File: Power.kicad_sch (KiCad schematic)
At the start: 16 parts, among them Q1 PMH950UPEH, U5 AP63205WU-7, U7 MCP1700T-3302E/TT

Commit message: 2nd rev schematic done
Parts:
- removed C10, C9: 1uF, Capacitor_SMD:C_0402_1005Metric, symbol Device:C_Small
- removed C4: 100nF, Capacitor_SMD:C_0402_1005Metric, symbol Device:C_Small
- removed C6, C7: 22uF, Capacitor_SMD:C_0805_2012Metric, symbol Device:C_Small
- removed U5: AP63205WU-7, SproutSenseFootprints:SOIC_05WU-7_DIO, symbol SproutSense:AP63205WU-7
- removed U7: MCP1700T-3302E/TT, SproutSenseFootprints:SOT-23_MC_MCH, symbol SproutSense:MCP1700T-3302E_TT
- added C11, C15, C16, C5: 22uF, Capacitor_SMD:C_0805_2012Metric, symbol Device:C_Small
- added C17: 10n, Capacitor_SMD:C_0201_0603Metric, symbol Device:C_Small
- added L3: 2.2u, SproutSenseFootprints:IND_VLS3012CX-2R2M-1, symbol Device:L_Small
- added R13: 9.31k, Resistor_SMD:R_0402_1005Metric, symbol Device:R_Small_US
- added R15: 7.5k, Resistor_SMD:R_0402_1005Metric, symbol Device:R_Small_US
- added R16, R22: 100k, Resistor_SMD:R_0402_1005Metric, symbol Device:R_US
- added R17: 154k, Resistor_SMD:R_0402_1005Metric, symbol Device:R_US
- added R21: 249k, Resistor_SMD:R_0402_1005Metric, symbol Device:R_US
- added R23, R24: 34k, Resistor_SMD:R_0402_1005Metric, symbol Device:R_US
- added U6: TPS629203DRL, SproutSenseFootprints:SOT5X3-8_DRL_TEX, symbol SproutSense:TPS629203DRL
- added U9: TPS629206DRLR, SOT5X3-8_DRL_TEX, symbol SproutSense:TPS629206DRLR
- C3: value 22uF -> 10n; footprint Capacitor_SMD:C_0805_2012Metric -> Capacitor_SMD:C_0201_0603Metric; Distributor Prt # 490-GRM21BZ71A226ME15LCT-ND -> 490-3194-1-ND; Manuf Prt # GRM21BZ71A226ME15L -> GRM033R71A103KA01D
- L1: value 4.7uH -> 2.2u; footprint SproutSenseFootprints:IND_TAIYO_NRS6028_TAY -> SproutSenseFootprints:IND_VLS3012CX-2R2M-1; Distributor Prt # 587-2943-1-ND -> 445-180922-1-ND; Manuf Prt # NRS6028T4R7MMGK -> VLS3012CX-2R2M-1
- R7: value 4.7k -> 7.5k; Distributor Prt # 311-4.7KJRCT-ND -> 311-7.50KLRCT-ND; Manuf Prt # RC0402JR-074K7L -> RC0402FR-077K5L
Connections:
- net +3V3: now also C3.1, L1.2, C11.1, R16.2, R17.1, U6.3 (VOS)
- net +5V: now also C16.1, C17.1, L3.2, R21.1, R22.2, U9.3 (VOS); no longer L1.2
- net +BATT: now also C15.1, C5.1, U6.6 (VIN), U6.7 (EN), U9.6 (VIN); no longer C3.1
- net GND: now also C11.2, C15.2, C16.2, C17.2, C5.2, R13.1, R15.1, R23.2, R24.2, U6.5 (GND), U9.5 (GND)
- net at L1.1: now also U6.4 (SW)
- new net: R17.2, R24.1, U6.1 (FB/VSET)
- new net: R21.2, R23.1, U9.1 (FB/VSET)
- new net: R22.1, U9.2 (PG)
- new net: L3.1, U9.4 (SW)
- new net: R13.2, U9.8 (MODE/S-CONF)
- new net: R16.1, U6.2 (PG)
- new net: R15.2, U6.8 (MODE/S-CONF)
- new net PWR_ENA_5p0: U9.7 (EN)
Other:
- note added: "Li-Ion 18650 Batt 7.2V Nom Voltage"
- note added: "Max Voltage = 8.4V 8.4 * (4.7 / 12.2) = 3.24"
- note removed: "X7R"
- moved on the sheet: BT2, BT3, D11, Q1, R8, R9

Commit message: mostly routed
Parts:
- removed BT2, BT3: Battery_Cell, SproutSenseFootprints:Keystone_18650_Holder, symbol Device:Battery_Cell
- added J1: S2B-PH-K-S, SproutSenseFootprints:CONN_S2B-PH-K-S_JST, symbol Connector:Conn_01x02_Socket
- added TP14, TP15: TestPoint, TestPoint:TestPoint_Pad_D1.0mm, symbol Connector:TestPoint
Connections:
- net +3V3: now also TP14.1
- net +5V: now also TP15.1
- net BAT_POS: now also J1.2 (Pin_2)
- net GND: now also J1.1 (Pin_1)
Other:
- note added: "2S 7.4V LiPo Battery"
- note removed: "Li-Ion 18650 Batt 7.2V Nom Voltage"
- moved on the sheet: D11, Q1, R7, R8, R9

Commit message: edited silksceen
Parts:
- added TP7: TestPoint, TestPoint:TestPoint_Pad_D1.0mm, symbol Connector:TestPoint
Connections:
- net GND: now also TP7.1
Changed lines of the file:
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@@
+	)
+	(junction
+		(at 199.39 120.65)
+		(diameter 0)
+		(color 0 0 0 0)
 	)
 	(junction
@@
 		(pts
 			(xy 67.31 99.06) (xy 67.31 104.14)
+		)
+		(stroke
+			(width 0)
+			(type default)
+		)
+	)
+	(wire
+		(pts
+			(xy 199.39 107.95) (xy 199.39 120.65)
 		)
 		(stroke
@@
 					(unit 1)
 				)
+			)
+		)
+	)
+	(symbol
+		(lib_id "Connector:TestPoint")
+		(at 199.39 107.95 0)
+		(unit 1)
+		(exclude_from_sim no)
+		(in_bom yes)
+		(on_board yes)
+		(dnp no)
+		(property "Reference" "TP7"
+			(at 197.866 102.87 0)
+			(effects
+				(font
+					(size 1.27 1.27)
+				)
+				(justify left)
+			)
+		)
+		(property "Value" "TestPoint"
+			(at 201.93 105.9179 0)
+			(effects
+				(font
+					(size 1.27 1.27)
+				)
+				(justify left)
+				(hide yes)
+			)
+		)
+		(property "Footprint" "TestPoint:TestPoint_Pad_D1.0mm"
+			(at 204.47 107.95 0)
+			(effects
+				(font
+					(size 1.27 1.27)
+				)
+				(hide yes)
+			)
+		)
+		(property "Datasheet" "~"
+			(at 204.47 107.95 0)
+			(effects
+				(font
+					(size 1.27 1.27)
+				)
+				(hide yes)
+			)
+		)
+		(property "Description" "test point"
+			(at 199.39 107.95 0)
+			(effects
+				(font
+					(size 1.27 1.27)
+				)
+				(hide yes)
+			)
+		)
+		(property "MAXIMUM_PACKAGE_HEIGHT" ""
+			(at 199.39 107.95 0)
+			(effects
+				(font
+					(size 1.27 1.27)
+				)
+				(hide yes)
+			)
+		)
+		(pin "1"
+		)
+		(instances
+			(project "SproutSync_SensorNode"
+				(path "/6b347550-6a02-4d2d-97d7-e1cbb1403859/8aac59c9-744f-46ff-a9bf-5095a50423d5"
+					(reference "TP7")
+					(unit 1)
+				)

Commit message: finished rev1
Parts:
- removed TP14, TP15: TestPoint, TestPoint:TestPoint_Pad_D1.0mm, symbol Connector:TestPoint
- added R25: 100m, Resistor_SMD:R_0603_1608Metric, symbol Device:R_Small_US
- added TP11, TP8: TestPoint, TestPoint:TestPoint_Pad_D1.0mm, symbol Connector:TestPoint
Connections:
- net +BATT: now also R25.2, TP11.1; no longer D11.1
- new net: D11.1, R25.1, TP8.1
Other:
- note added: "rsense for power testing"
- moved on the sheet: C11, C16, C17, C3

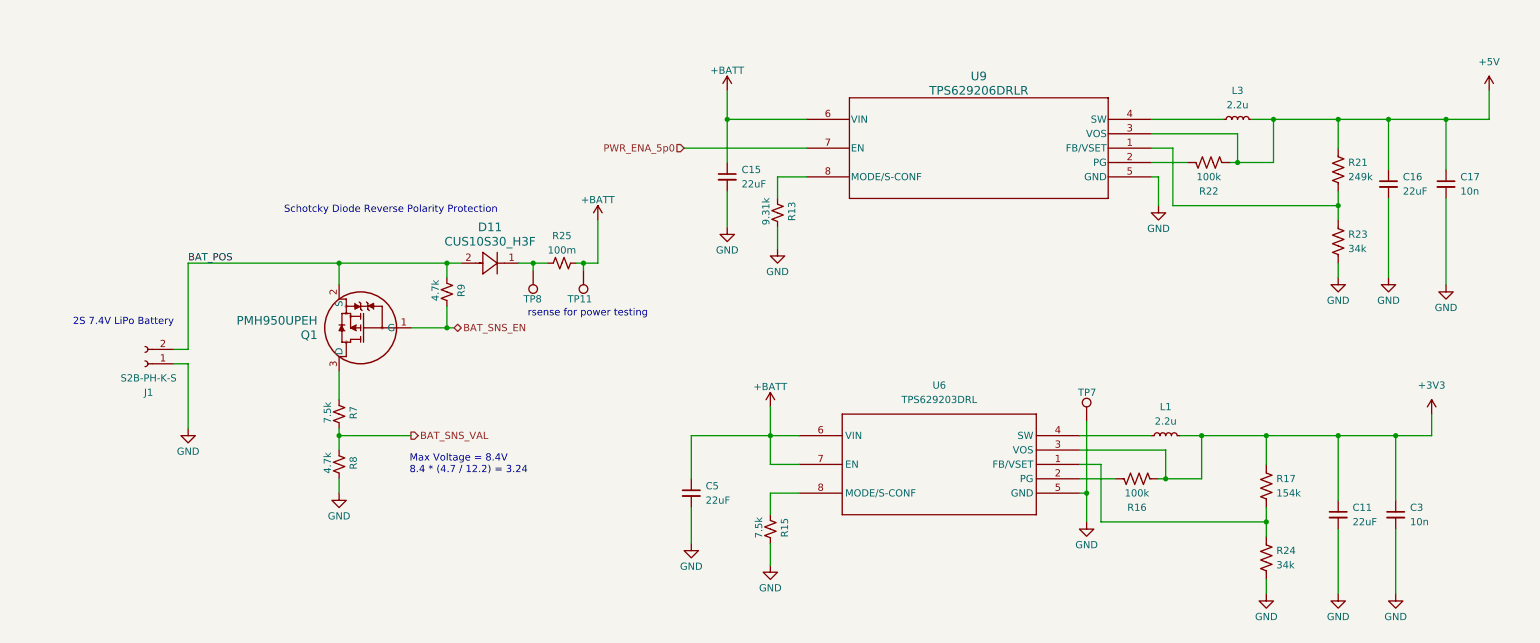
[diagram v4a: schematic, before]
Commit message: Removed via in pads
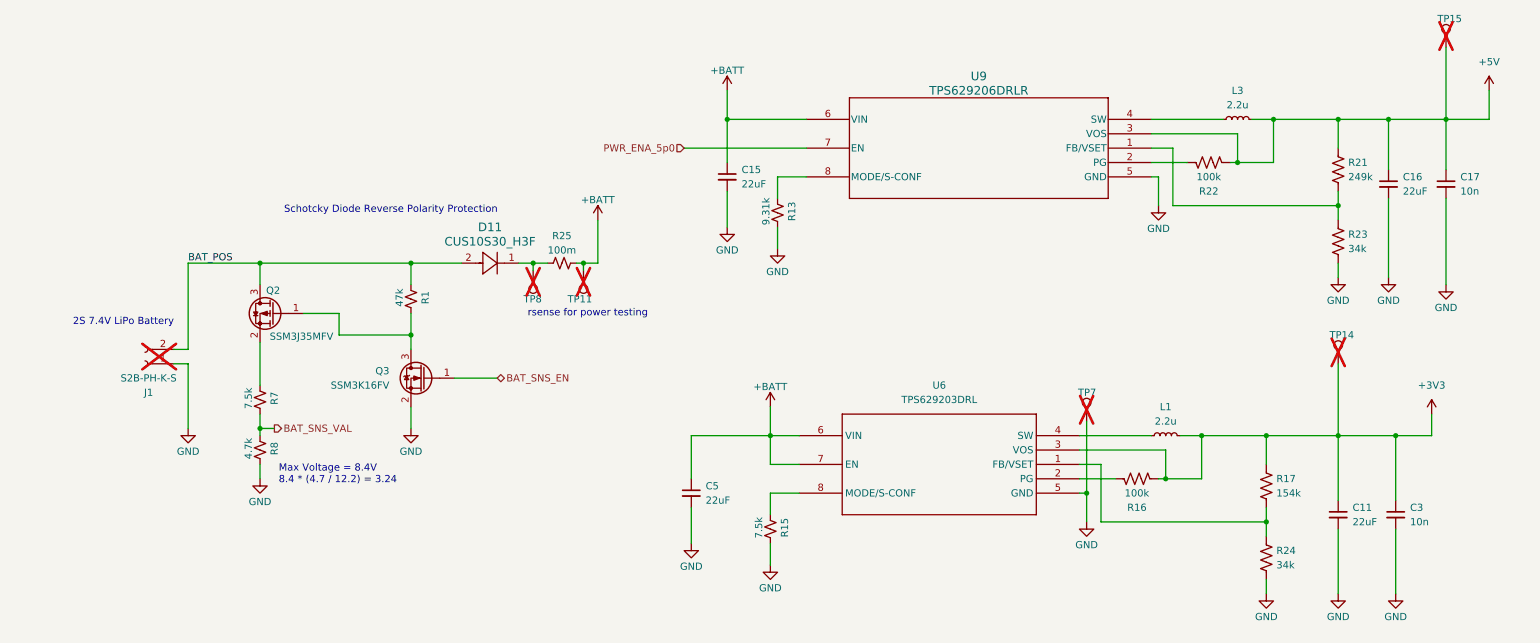
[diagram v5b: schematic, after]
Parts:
- removed Q1: PMH950UPEH, SproutSenseFootprints:QPMOS1G2S3d_SOT8001_NEX, symbol SproutSense:PMH950UPEH
- removed R9: 4.7k, Resistor_SMD:R_0402_1005Metric, symbol Device:R_Small_US
- added Q2: SSM3J35MFV, SproutSenseFootprints:VESM_TOS, symbol Transistor_FET:Q_PMOS_GSD
- added Q3: SSM3K16FV, SproutSenseFootprints:VESM_TOS, symbol Transistor_FET_Other:Q_NMOS_Depletion_GSD
- added R1: 47k, Resistor_SMD:R_0402_1005Metric, symbol Device:R_Small_US
- added TP14, TP15: TestPoint, TestPoint:TestPoint_Pad_D1.0mm, symbol Connector:TestPoint
- J1: now not fitted
- TP11, TP7, TP8: now not fitted; now left out of the parts list
- U9: footprint SOT5X3-8_DRL_TEX -> SproutSenseFootprints:SOT5X3-8_DRL_TEX
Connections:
- net +3V3: now also TP14.1
- net +5V: now also TP15.1
- net BAT_POS: now also Q2.3 (D), R1.2
- net BAT_SNS_EN: now also Q3.1 (G)
- net GND: now also Q3.2 (S)
- net at R7.2: now also Q2.2 (S)
- new net: Q2.1 (G), Q3.3 (D), R1.1
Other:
- moved on the sheet: R7, R8
